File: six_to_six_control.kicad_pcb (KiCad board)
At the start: 2 copper layers, 99.1 x 74.9 mm, 16 parts, among them J1 relays, J2 relays, J3 relays, J4 relays, J5 relays, J6 relays, J7 12V Power, U1 RS-485_module

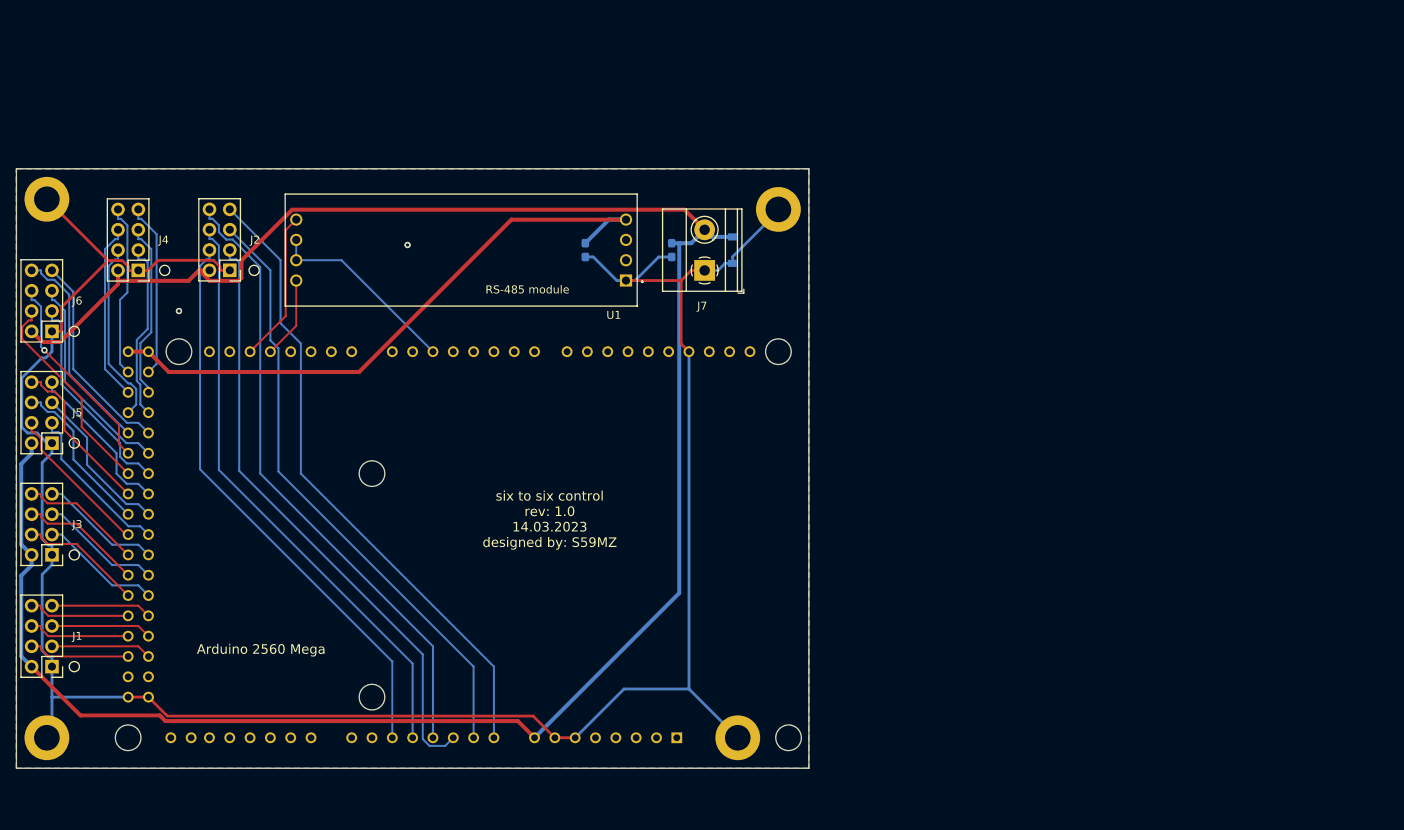
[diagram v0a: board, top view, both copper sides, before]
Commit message: added db9 and Ethernet module
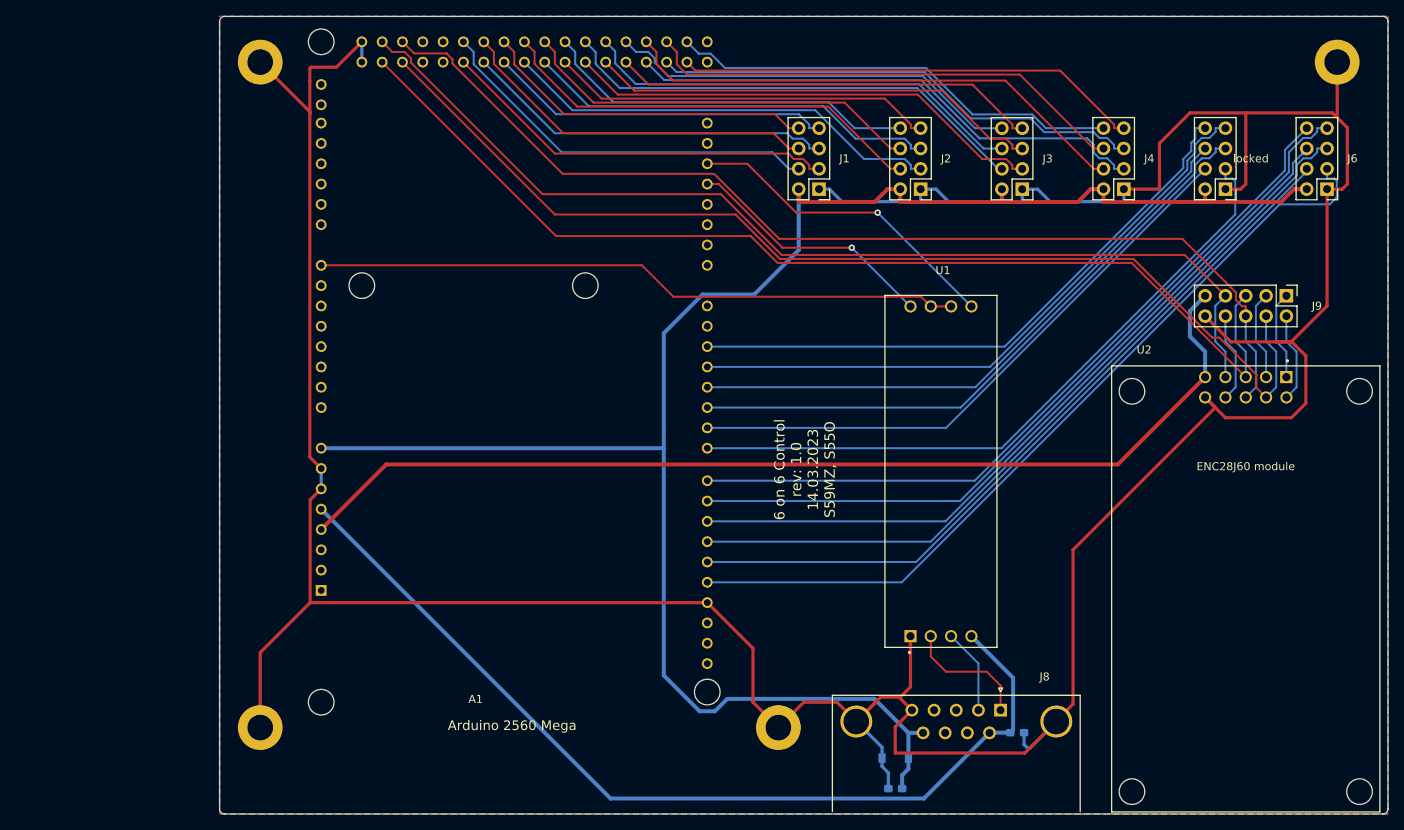
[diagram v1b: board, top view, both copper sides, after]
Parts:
- removed J7: 12V Power, TerminalBlock_Phoenix:TerminalBlock_Phoenix_MKDS-1,5-2-5.08_1x02_P5.08mm_Horizontal
- added J8: DB9_Female_MountingHoles, Connector_Dsub:DSUB-9_Female_Horizontal_P2.77x2.84mm_EdgePinOffset9.90mm_Housed_MountingHolesOffset11.32mm, F.Cu at (173.8, 126.1)
- added J9: Conn_02x05_Odd_Even, Connector_PinHeader_2.54mm:PinHeader_2x05_P2.54mm_Vertical, F.Cu at (209.6, 74.3)
- added U2: ENC28J60_module, Library:ENC28J60_module, F.Cu at (209.6, 84.5)
- moved J6 160.4 mm to (214.6, 61.0)
- moved locked 150.1 mm to (201.9, 61.0)
- moved J3 129.6 mm to (176.5, 61.0)
- moved J4 123.6 mm to (189.2, 61.0)
- moved J1 112.9 mm to (151.1, 61.0)
- moved J2 86.9 mm to (163.8, 61.0)
- moved C2 80.9 mm to (175.9, 128.9), turned to 0 degrees
- moved A1 78.7 mm to (137.2, 45.1), turned to 0 degrees
- moved C1 72.9 mm to (160.7, 135.9), turned to 180 degrees
- moved H2 72.2 mm to (215.9, 45.1)
- moved D1 66.7 mm to (160.7, 132.1), turned to 180 degrees
- moved U1 56.9 mm to (162.6, 116.8), turned to 90 degrees
- moved H1 31.7 mm to (81.3, 45.1)
- moved H3 26.7 mm to (81.3, 128.3)
- moved H4 5.24 mm to (146.1, 128.3)
- renumbered J5 to locked
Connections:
- A1 pad 10: unconnected-(A1-Pad10) -> /d10
- A1 pad 11: unconnected-(A1-Pad11) -> /d11
- A1 pad 12: unconnected-(A1-Pad12) -> /d12
- A1 pad 13: unconnected-(A1-Pad13) -> /d13
- A1 pad 2: Net-(A1-Pad2) -> /d2
- A1 pad 3: unconnected-(A1-Pad3) -> /d3
- A1 pad 3V3: unconnected-(A1-Pad3V3) -> +3V3
- A1 pad 4: unconnected-(A1-Pad4) -> /d4
- A1 pad 46: /d46 -> unconnected-(A1-Pad46)
- A1 pad 47: /d47 -> unconnected-(A1-Pad47)
- A1 pad 48: /d48 -> unconnected-(A1-Pad48)
- A1 pad 49: /d49 -> unconnected-(A1-Pad49)
- A1 pad 5: unconnected-(A1-Pad5) -> /d5
- A1 pad 50: /d50 -> /miso
- A1 pad 51: /d51 -> /sck
- A1 pad 52: unconnected-(A1-Pad52) -> /mosi
- A1 pad 53: unconnected-(A1-Pad53) -> /cs
- A1 pad 5V_1: unconnected-(A1-Pad5V_1) -> +5V
- A1 pad 5V_2: +5V -> unconnected-(A1-Pad5V_2)
- A1 pad 5V_3: +5V -> unconnected-(A1-Pad5V_3)
- A1 pad 6: unconnected-(A1-Pad6) -> /d6
- A1 pad 7: unconnected-(A1-Pad7) -> /d7
- A1 pad 8: unconnected-(A1-Pad8) -> /d8
- A1 pad 9: unconnected-(A1-Pad9) -> /d9
- A1 pad AD0: /d54 -> unconnected-(A1-PadAD0)
- A1 pad AD1: /d55 -> unconnected-(A1-PadAD1)
- A1 pad AD2: /d56 -> unconnected-(A1-PadAD2)
- A1 pad AD3: /d57 -> unconnected-(A1-PadAD3)
- A1 pad AD4: /d58 -> unconnected-(A1-PadAD4)
- A1 pad AD5: /d59 -> unconnected-(A1-PadAD5)
- A1 pad AD7: unconnected-(A1-PadAD7) -> /ad7
- J1 pad 3: /d50 -> /d44
- J1 pad 4: /d51 -> /d45
- J1 pad 5: /d48 -> /d42
- J1 pad 6: /d49 -> /d43
- J1 pad 7: /d46 -> /d40
- J1 pad 8: /d47 -> /d41
- J2 pad 3: /d56 -> /d38
- J2 pad 4: /d59 -> /d39
- J2 pad 5: /d55 -> /d36
- J2 pad 6: /d58 -> /d37
- J2 pad 7: /d54 -> /d34
- J2 pad 8: /d57 -> /d35
- J3 pad 3: /d44 -> /d32
- J3 pad 4: /d45 -> /d33
- J3 pad 5: /d42 -> /d30
- J3 pad 6: /d43 -> /d31
- J3 pad 7: /d40 -> /d28
- J3 pad 8: /d41 -> /d29
- J6 pad 3: /d32 -> /d13
- J6 pad 4: /d33 -> /d12
- J6 pad 5: /d30 -> /d11
- J6 pad 6: /d31 -> /d10
- J6 pad 7: /d28 -> /d9
- J6 pad 8: /d29 -> /d8
- U1 pad 2: unconnected-(U1-Pad2) -> Net-(J8-Pad1)
- U1 pad 3: unconnected-(U1-Pad3) -> Net-(J8-Pad2)
- U1 pad 6: Net-(A1-Pad2) -> /ad7
- U1 pad 7: Net-(A1-Pad2) -> /ad7
- locked pad 3: /d38 -> /d7
- locked pad 4: /d39 -> /d6
- locked pad 5: /d36 -> /d5
- locked pad 6: /d37 -> /d4
- locked pad 7: /d34 -> /d3
- locked pad 8: /d35 -> /d2
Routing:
- net GND: track 279.9 -> 467.8 mm, vias 2 -> 0
- net /miso: track 0.00 -> 137.5 mm
- net /mosi: track 0.00 -> 135.5 mm
- net /sck: track 0.00 -> 132.4 mm
- net +3V3: track 0.00 -> 130.1 mm
- net /cs: track 0.00 -> 130.1 mm
- net /d13: track 0.00 -> 103.2 mm
- net /d11: track 0.00 -> 98.9 mm
- net /d9: track 0.00 -> 98.5 mm
- net /d12: track 0.00 -> 95.5 mm
- net /d10: track 0.00 -> 95.4 mm
- net /d8: track 0.00 -> 94.7 mm
- net /d7: track 0.00 -> 84.9 mm
- net /ad7: track 0.00 -> 80.9 mm
- net /d54: track 79.7 -> 0.00 mm
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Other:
- board size 99.1 x 74.9 mm -> 146.1 x 99.7 mm
- board text added: "6 on 6 Control rev: 1.0 14.03.2023 S59MZ, S55O"
- board text removed: "RS-485 module"
- board text removed: "six to six control rev: 1.0 14.03.2023 designed by: S59MZ"

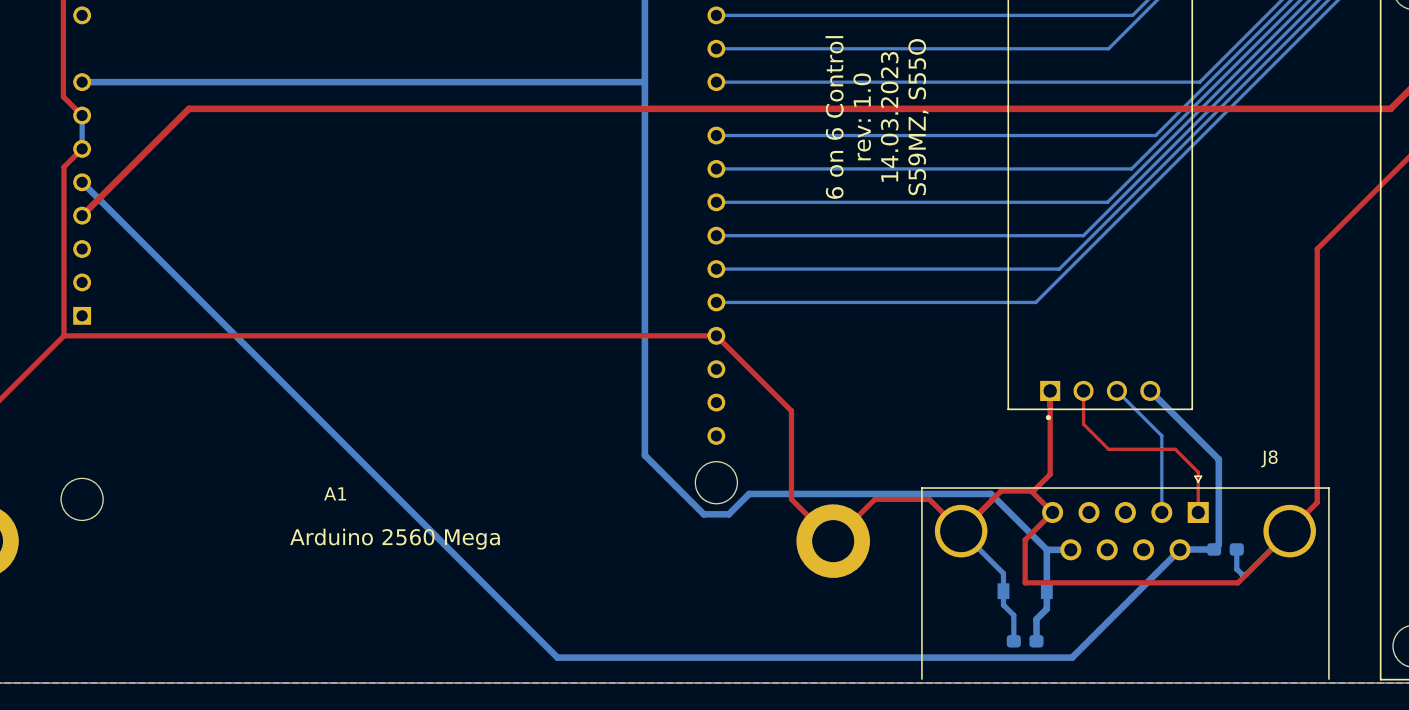
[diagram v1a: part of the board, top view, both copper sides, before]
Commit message: fixed db9 layout
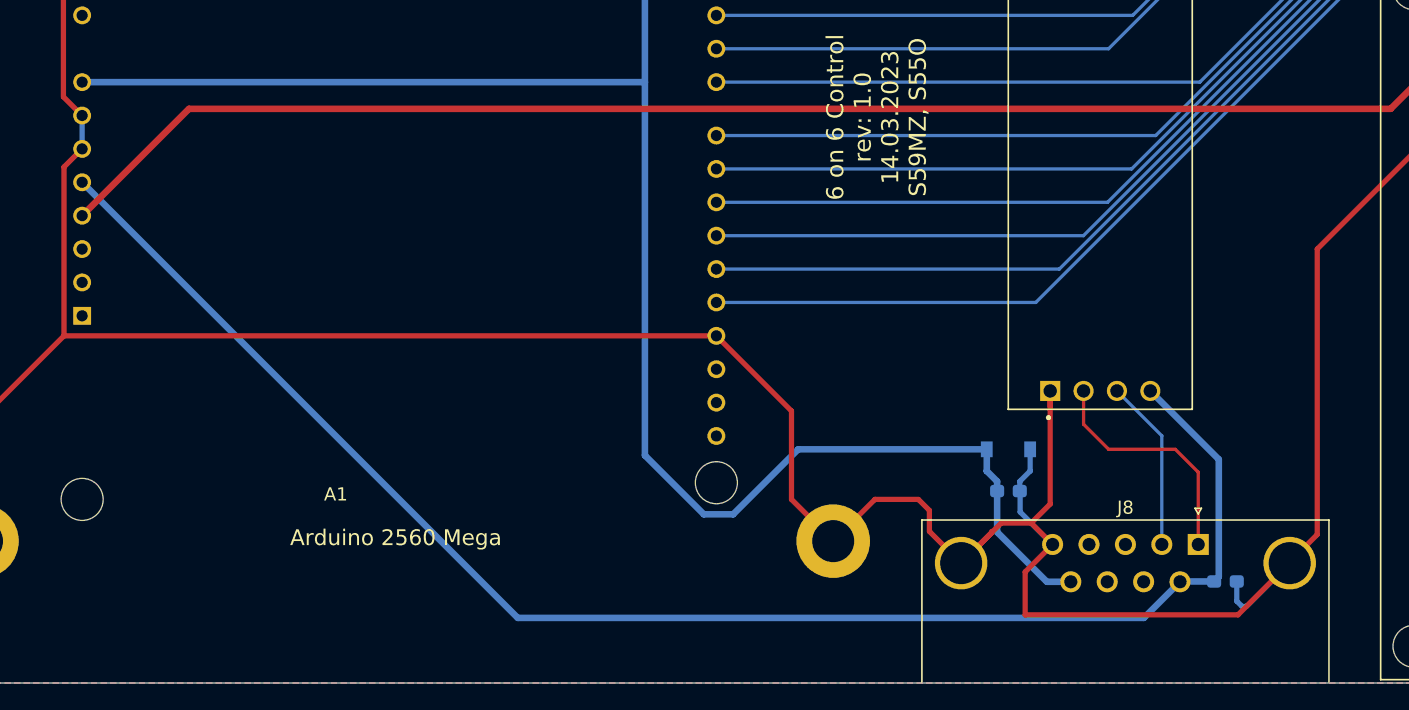
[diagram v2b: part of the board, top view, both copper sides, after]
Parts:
- J8: value DB9_Female_MountingHoles -> 5504F1-09S-02-03; footprint Connector_Dsub:DSUB-9_Female_Horizontal_P2.77x2.84mm_EdgePinOffset9.90mm_Housed_MountingHolesOffset11.32mm -> Connector_Dsub:DSUB-9_Female_Horizontal_P2.77x2.84mm_EdgePinOffset7.70mm_Housed_MountingHolesOffset9.12mm
- moved C1 11.5 mm to (159.4, 124.5), turned to 0 degrees
- moved D1 10.9 mm to (159.4, 121.3), turned to 0 degrees
- moved C2 2.43 mm to (175.9, 131.3)
- moved J8 2.43 mm to (173.8, 128.5)
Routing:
- net GND: track 467.8 -> 473.1 mm
- net Net-(J8-Pad2): track 10.7 -> 13.1 mm
- net Net-(J8-Pad1): track 15.8 -> 18.3 mm
- net +5V: track 118.9 -> 117.8 mm

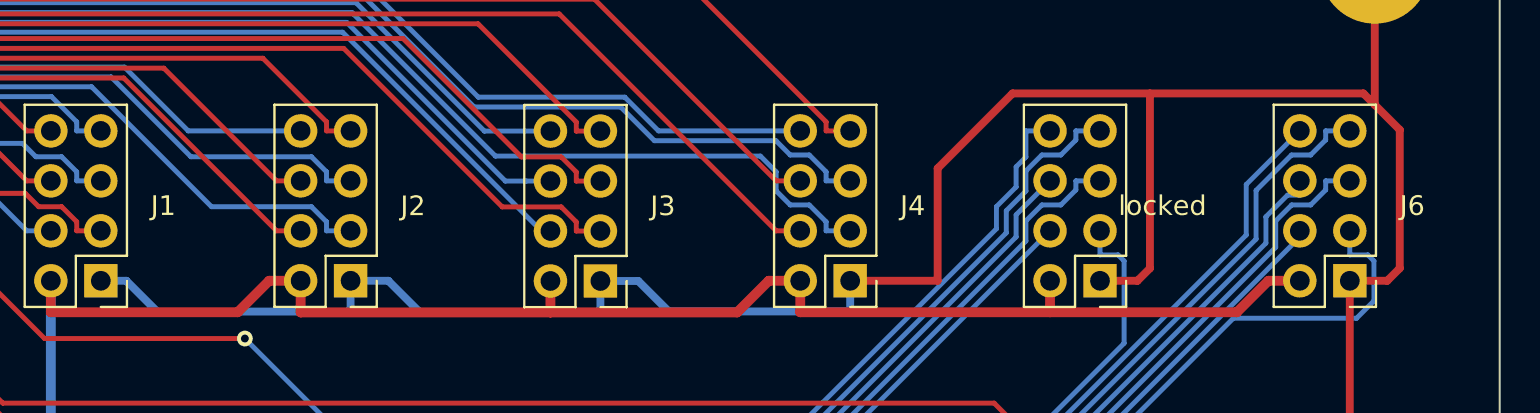
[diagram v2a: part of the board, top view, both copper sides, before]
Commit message: reannotate connectors
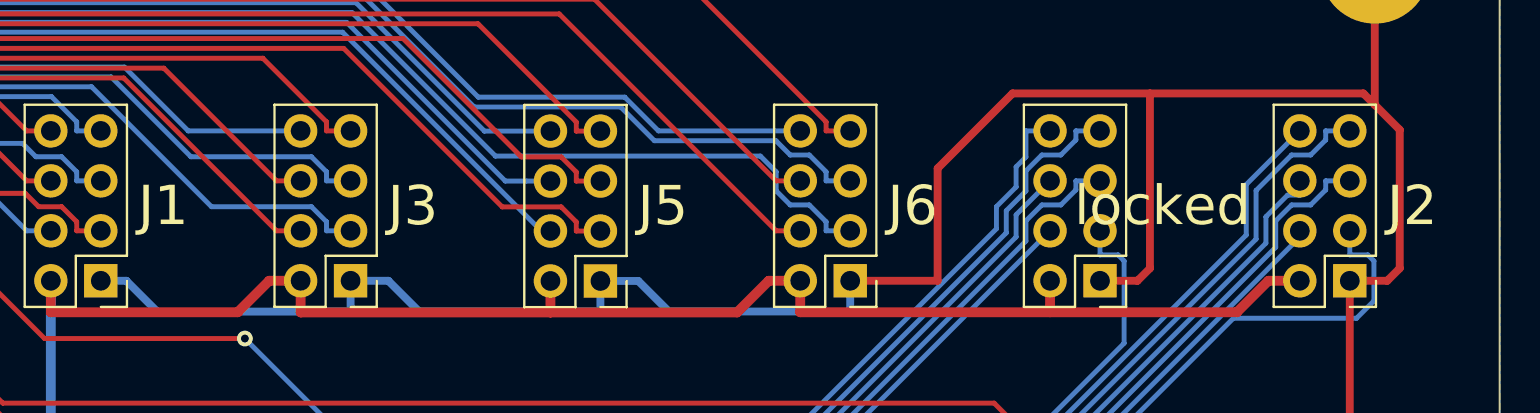
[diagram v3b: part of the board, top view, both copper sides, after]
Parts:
- renumbered J6 to J2, J2 to J3, J3 to J5, J4 to J6
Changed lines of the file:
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@@
     (property "Sheetname" "")
     (attr through_hole)
-    (fp_text reference locked "J5" (at -3.175 3.81) (layer "F.SilkS")
-      (effects (font (size 1 1) (thickness 0.15)))
+    (fp_text reference locked "J4" (at -3.175 3.81) (layer "F.SilkS")
+      (effects (font (size 2 2) (thickness 0.3)))
     )
     (fp_text value "relays" (at 1.27 9.95) (layer "F.Fab")
@@
     (attr through_hole)
     (fp_text reference "J1" (at -3.175 3.81) (layer "F.SilkS")
-      (effects (font (size 1 1) (thickness 0.15)))
+      (effects (font (size 2 2) (thickness 0.3)))
     )
     (fp_text value "relays" (at 1.27 9.95) (layer "F.Fab")
@@
     (property "Sheetname" "")
     (attr through_hole)
-    (fp_text reference "J4" (at -3.175 3.81) (layer "F.SilkS")
-      (effects (font (size 1 1) (thickness 0.15)))
+    (fp_text reference "J6" (at -3.175 3.81) (layer "F.SilkS")
+      (effects (font (size 2 2) (thickness 0.3)))
     )
     (fp_text value "relays" (at 1.27 9.95) (layer "F.Fab")
@@
     (property "Sheetname" "")
     (attr through_hole)
-    (fp_text reference "J2" (at -3.17 3.8) (layer "F.SilkS")
-      (effects (font (size 1 1) (thickness 0.15)))
+    (fp_text reference "J3" (at -3.17 3.8) (layer "F.SilkS")
+      (effects (font (size 2 2) (thickness 0.3)))
     )
     (fp_text value "relays" (at 1.27 9.95) (layer "F.Fab")
@@
     (property "Sheetname" "")
     (attr through_hole)
-    (fp_text reference "J3" (at -3.175 3.81) (layer "F.SilkS")
-      (effects (font (size 1 1) (thickness 0.15)))
+    (fp_text reference "J5" (at -3.175 3.81) (layer "F.SilkS")
+      (effects (font (size 2 2) (thickness 0.3)))
     )
     (fp_text value "relays" (at 1.27 9.95) (layer "F.Fab")
@@
     (property "Sheetname" "")
     (attr through_hole)
-    (fp_text reference "J6" (at -3.175 3.81) (layer "F.SilkS")
-      (effects (font (size 1 1) (thickness 0.15)))
+    (fp_text reference "J2" (at -3.175 3.81) (layer "F.SilkS")
+      (effects (font (size 2 2) (thickness 0.3)))
     )
     (fp_text value "relays" (at 1.27 9.95) (layer "F.Fab")
